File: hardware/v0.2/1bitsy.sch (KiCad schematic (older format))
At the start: 30 parts, among them J1 BOOT, P24 USB_OTG, SW1 TACT, U1 VREG_3V3, U2 STM32F415RGT, X2 25MHz, X3 JTAG-10

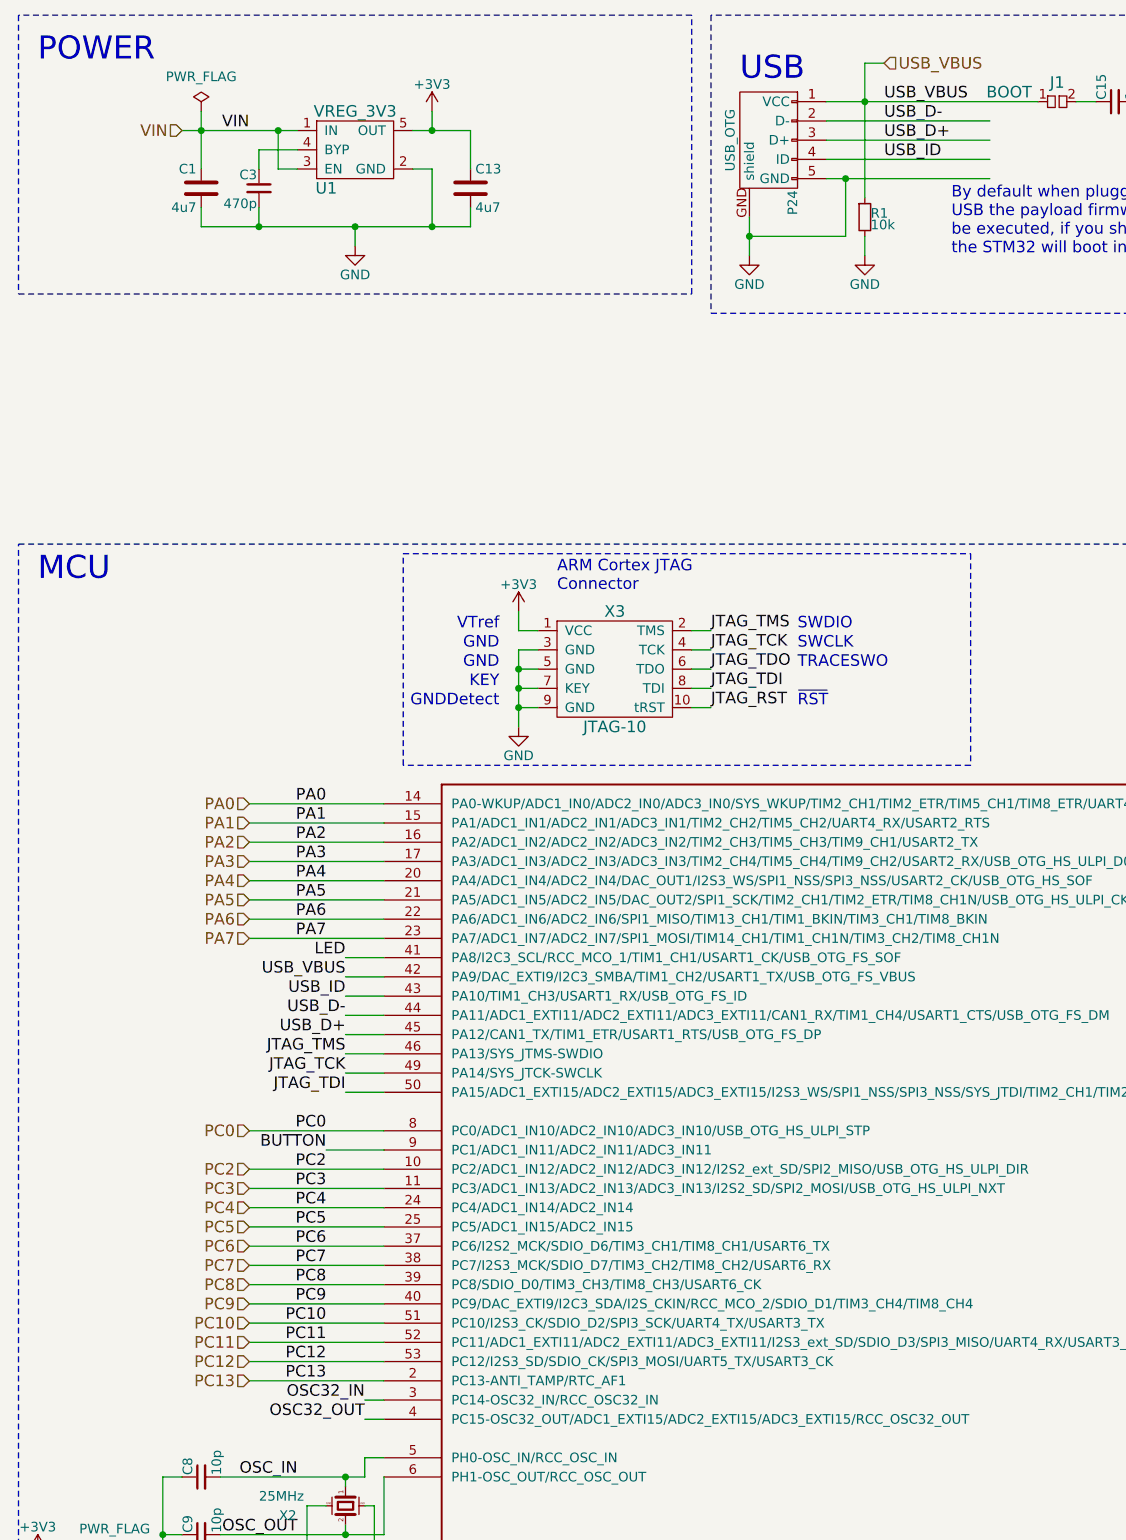
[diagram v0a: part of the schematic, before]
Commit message: Added FPGA. (iCEBreaker circuit, iCE40UP5k)
The iCE40UP5k FPGA (mostly iCEBreaker-bitsy circuit) is now connected
between the 1Bitsy STM32F415 mcu and the LCD. The default bitstream
should pass the signals through resulting in transparent operation. This
new FPGA will allow the transparent use of differet LCDs with different
controllers than the ILI9341. It will also allow the implementation of
FPGA based graphic accelerators and game emulators/implementations.
Addition of the FPGA fabric into the mix will increase the amount of
different interesting projects on this platform by a huge factor.
Especially because the iCE40 can benefit from the open source Yosys,
arachnepnr, icestorm toolchain!
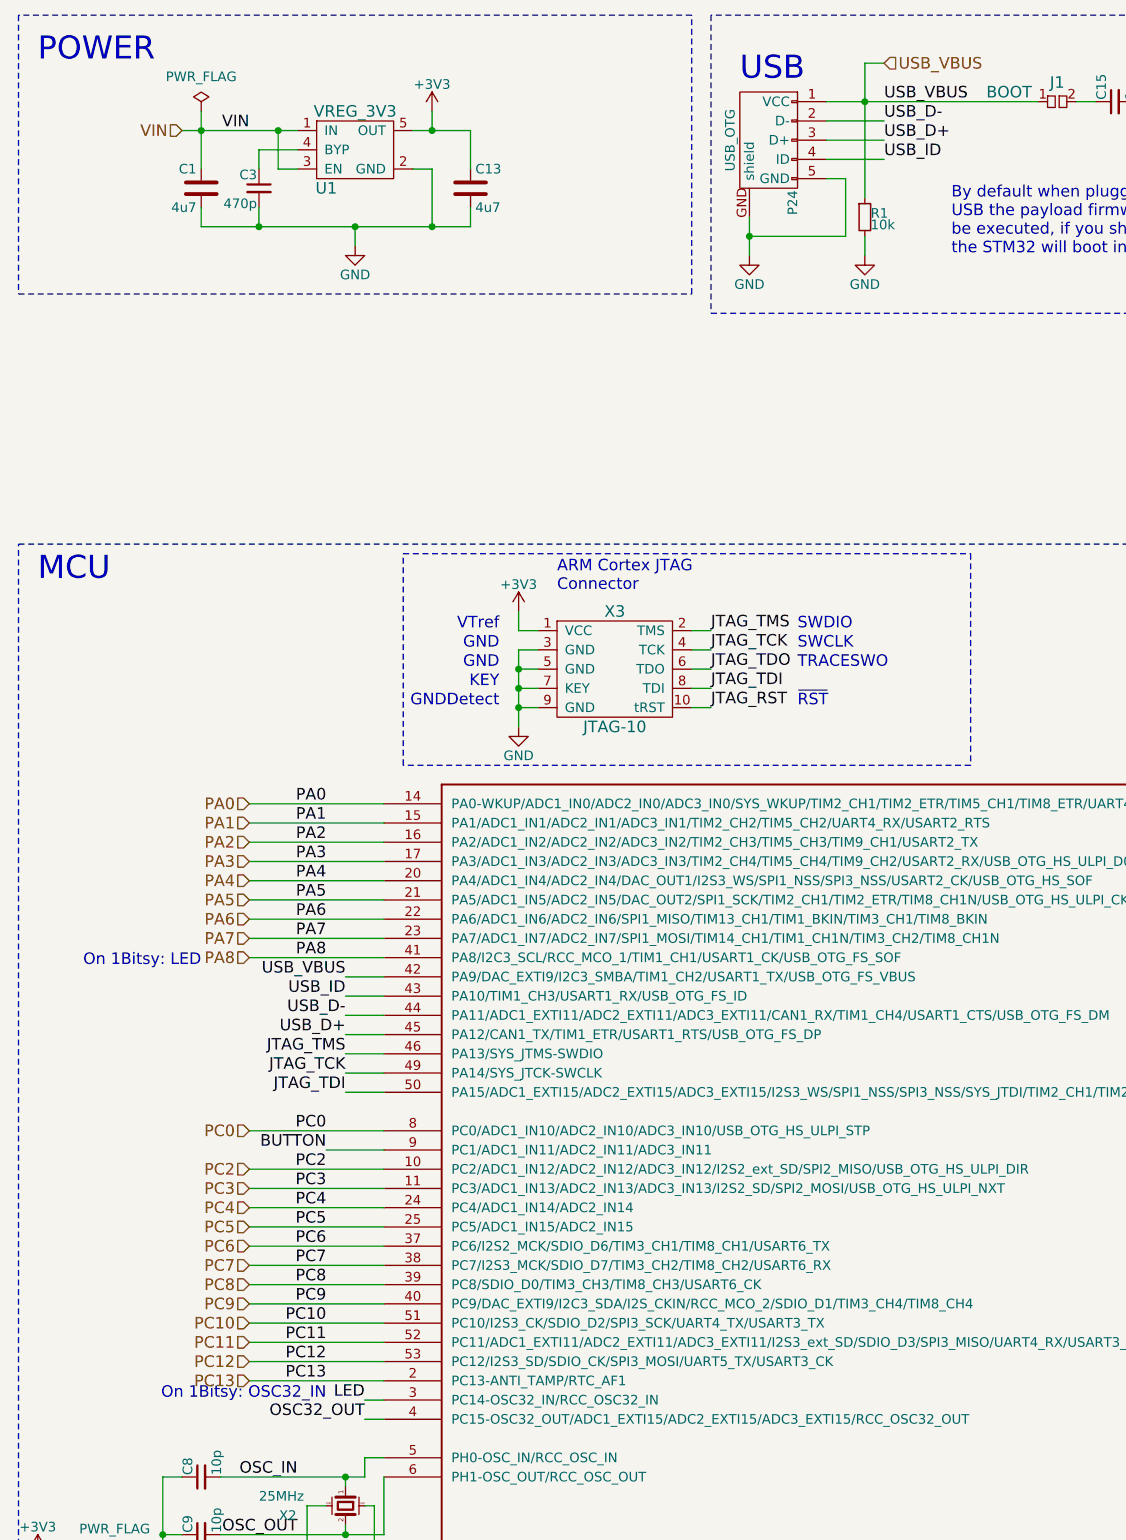
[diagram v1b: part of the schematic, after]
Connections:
- net OSC32_IN is gone; now on net LED: U2.3 (PC14-OSC32_IN/RCC_OSC32_IN)
- net LED: no longer U2.41 (PA8/I2C3_SCL/RCC_MCO_1/TIM1_CH1/USART1_CK/USB_OTG_FS_SOF)
- new net PA8: U2.41 (PA8/I2C3_SCL/RCC_MCO_1/TIM1_CH1/USART1_CK/USB_OTG_FS_SOF)
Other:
- note added: "On 1Bitsy: LED"
- note added: "On 1Bitsy: OSC32_IN"
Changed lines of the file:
@@
 $Descr A3 16535 11693
 encoding utf-8
-Sheet 2 2
+Sheet 2 3
 Title "1BitSy"
 Date ""
@@
 	1750 5350 2450 5350
 Wire Wire Line
-	2250 5450 2450 5450
+	1750 5450 2450 5450
 Wire Wire Line
 	2450 5550 2250 5550
@@
 	6350 1000 6450 1000
 Wire Wire Line
-	4750 1100 5600 1100
-Wire Wire Line
-	4750 1200 5600 1200
+	4750 1100 5050 1100
+Wire Wire Line
+	4750 1200 5050 1200
 Wire Wire Line
 	9750 2050 9750 2150
@@
 Text Label 2250 5550 2    60   ~ 0
 USB_VBUS
-Text Label 2250 5450 2    60   ~ 0
-LED
 Text Label 2150 5350 2    60   ~ 0
 PA7
@@
 PA1
 Wire Wire Line
-	4750 1300 5600 1300
+	4750 1300 5050 1300
 Text Label 5050 1300 0    60   ~ 0
 USB_ID
@@
 VIN
 Text Label 2350 7750 2    60   ~ 0
-OSC32_IN
+LED
 Text Label 2350 7850 2    60   ~ 0
 OSC32_OUT
@@
 Wire Notes Line
 	550  550  550  2000
-Connection ~ 4850 1400
 Text Label 14600 8250 0    60   ~ 0
 VBAT
@@
 Wire Wire Line
 	1300 8150 1300 8450
-Wire Wire Line
-	4850 1400 5600 1400
 Wire Wire Line
 	4950 1000 5850 1000
@@
 Text HLabel 1750 7550 0    60   Input ~ 0
 PC12
-Text HLabel 1750 7650 0    60   Input ~ 0
-PC13
 Text HLabel 14050 6350 2    60   Input ~ 0
 PD2
@@
 Text HLabel 14050 6150 2    60   Input ~ 0
 PB15
+Text HLabel 1750 5450 0    60   Input ~ 0
+PA8
+Text HLabel 1750 7650 0    60   Input ~ 0
+PC13
+Text Notes 2150 7750 2    60   ~ 0
+On 1Bitsy: OSC32_IN
+Text Notes 1500 5500 2    60   ~ 0
+On 1Bitsy: LED
+Text Label 2150 5450 2    60   ~ 0
+PA8
 $EndSCHEMATC

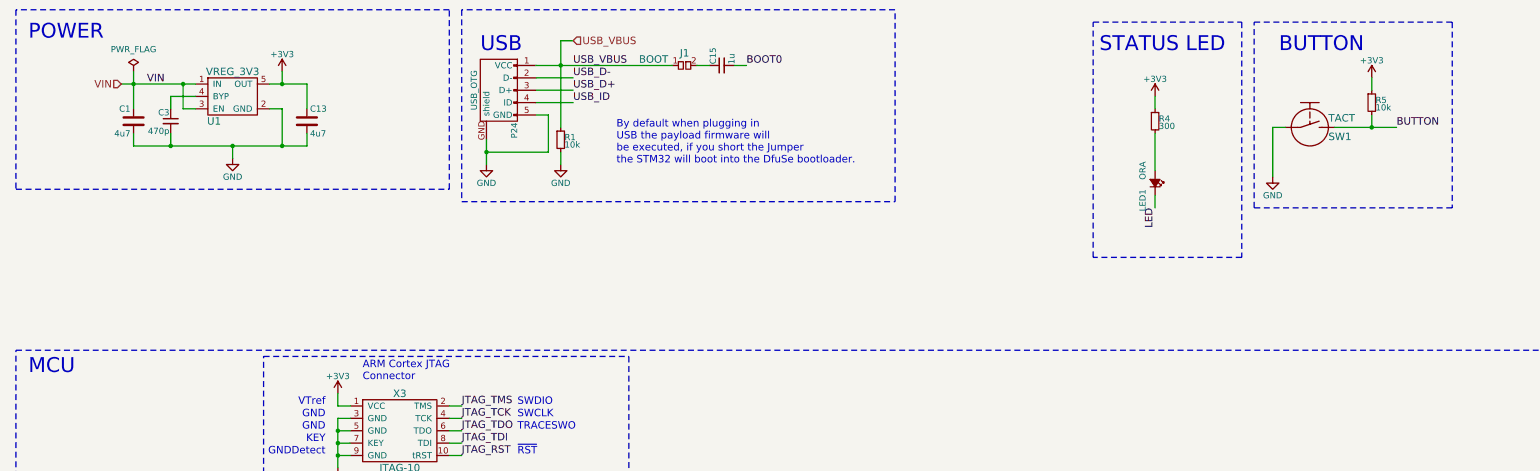
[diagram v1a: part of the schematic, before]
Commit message: Added MEMS microphone input.
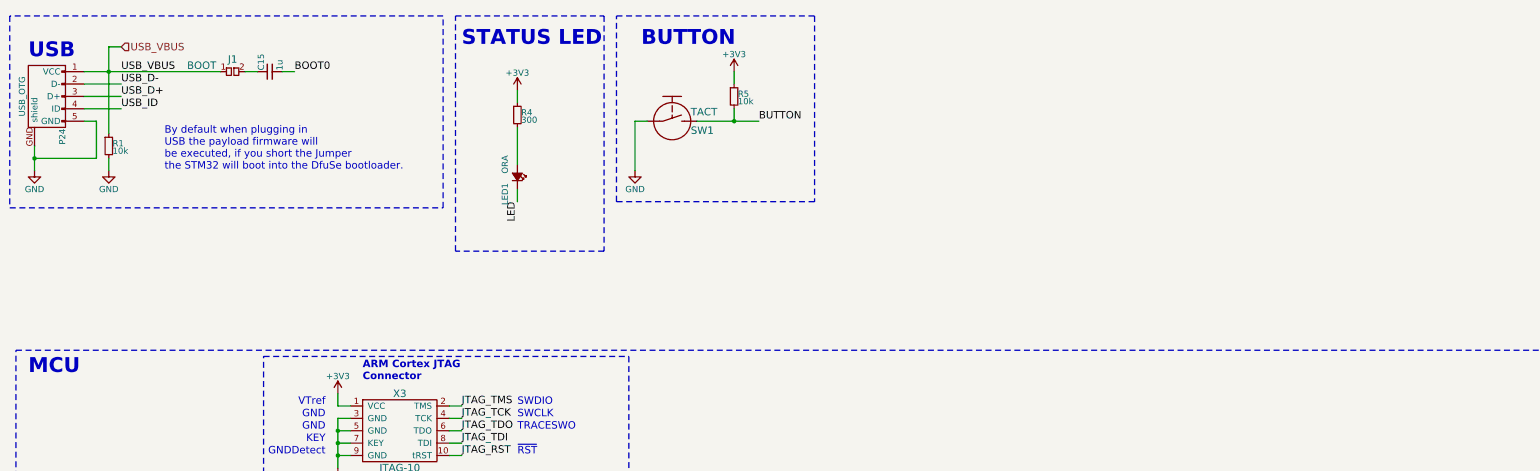
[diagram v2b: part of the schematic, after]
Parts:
- removed C1, C13: 4u7, pkl_dipol:C_0603, symbol pkl_device:pkl_C
- removed C3: 470p, pkl_dipol:C_0402, symbol pkl_device:pkl_C_Small
- removed U1: VREG_3V3, pkl_housings_sot:SOT-23-5, symbol pkl_device:pkl_VREG_5PIN_FIXED
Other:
- note removed: "POWER"
- moved on the sheet: C15, J1, LED1, P24, R1, R4, R5, SW1
